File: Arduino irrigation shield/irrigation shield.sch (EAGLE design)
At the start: 3 parts, among them IC1 74LS595N, U1 ARDUINOR3-DIMENSION

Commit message: work in progress
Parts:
- added DZ1: LB10, led:LB10
- added R1: 4.7k, resistor:R-US_0207/7
- added S1: Next Zone, switch-omron:10-XX
- added SJ1, SJ2, SJ3, SJ4, SJ5, SJ6, SJ7: (no value), jumper:SJ
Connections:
- new net N$1: IC1A.SCK, U1.D6
- new net N$2: IC1A.RCK, U1.D5
- new net N$3: IC1A.SER, U1.D4
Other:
- moved on the sheet: IC1
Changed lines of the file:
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@@
 <part name="IC1" library="74xx-us" deviceset="74*595" device="N" technology="LS"/>
 <part name="T1" library="transistor" deviceset="*-NPN-" device="TO92"/>
+<part name="R1" library="resistor" deviceset="R-US_" device="0207/7" value="4.7k"/>
+<part name="DZ1" library="led" deviceset="LB10" device=""/>
+<part name="SJ1" library="jumper" deviceset="SJ" device=""/>
+<part name="SJ2" library="jumper" deviceset="SJ" device=""/>
+<part name="SJ3" library="jumper" deviceset="SJ" device=""/>
+<part name="SJ4" library="jumper" deviceset="SJ" device=""/>
+<part name="SJ5" library="jumper" deviceset="SJ" device=""/>
+<part name="SJ6" library="jumper" deviceset="SJ" device=""/>
+<part name="SJ7" library="jumper" deviceset="SJ" device=""/>
+<part name="S1" library="switch-omron" deviceset="10-XX" device="" value="Next Zone"/>
 </parts>
 <sheets>
@@
 <instances>
 <instance part="U1" gate="G$1" x="10.16" y="58.42"/>
-<instance part="IC1" gate="A" x="86.36" y="66.04"/>
+<instance part="IC1" gate="A" x="20.32" y="116.84" rot="R90"/>
 <instance part="T1" gate="G$1" x="71.12" y="30.48"/>
+<instance part="R1" gate="G$1" x="58.42" y="30.48"/>
+<instance part="DZ1" gate="-1" x="48.26" y="91.44"/>
+<instance part="DZ1" gate="-2" x="63.5" y="91.44"/>
+<instance part="DZ1" gate="-3" x="78.74" y="91.44"/>
+<instance part="DZ1" gate="-4" x="93.98" y="91.44"/>
+<instance part="DZ1" gate="-5" x="109.22" y="91.44"/>
+<instance part="DZ1" gate="-6" x="48.26" y="73.66"/>
+<instance part="DZ1" gate="-7" x="63.5" y="73.66"/>
+<instance part="DZ1" gate="-8" x="78.74" y="73.66"/>
+<instance part="DZ1" gate="-9" x="93.98" y="73.66"/>
+<instance part="DZ1" gate="-10" x="109.22" y="73.66"/>
+<instance part="SJ1" gate="1" x="48.26" y="63.5"/>
+<instance part="SJ2" gate="1" x="60.96" y="63.5"/>
+<instance part="SJ3" gate="1" x="73.66" y="63.5"/>
+<instance part="SJ4" gate="1" x="86.36" y="63.5"/>
+<instance part="SJ5" gate="1" x="99.06" y="63.5"/>
+<instance part="SJ6" gate="1" x="111.76" y="63.5"/>
+<instance part="SJ7" gate="1" x="124.46" y="63.5"/>
+<instance part="S1" gate="1" x="-35.56" y="109.22"/>
 </instances>
 <busses>
 </busses>
 <nets>
+<net name="N$1" class="0">
+<segment>
+<pinref part="U1" gate="G$1" pin="D6"/>
+<pinref part="IC1" gate="A" pin="SCK"/>
+<wire x1="15.24" y1="88.9" x2="15.24" y2="106.68" width="0.1524" layer="91"/>
+</segment>
+</net>
+<net name="N$2" class="0">
+<segment>
+<pinref part="U1" gate="G$1" pin="D5"/>
+<wire x1="17.78" y1="88.9" x2="17.78" y2="99.06" width="0.1524" layer="91"/>
+<wire x1="17.78" y1="99.06" x2="22.86" y2="99.06" width="0.1524" layer="91"/>
+<pinref part="IC1" gate="A" pin="RCK"/>
+<wire x1="22.86" y1="99.06" x2="22.86" y2="106.68" width="0.1524" layer="91"/>
+</segment>
+</net>
+<net name="N$3" class="0">
+<segment>
+<pinref part="U1" gate="G$1" pin="D4"/>
+<wire x1="20.32" y1="88.9" x2="20.32" y2="96.52" width="0.1524" layer="91"/>
+<wire x1="20.32" y1="96.52" x2="10.16" y2="96.52" width="0.1524" layer="91"/>
+<pinref part="IC1" gate="A" pin="SER"/>
+<wire x1="10.16" y1="96.52" x2="10.16" y2="106.68" width="0.1524" layer="91"/>
+</segment>
+</net>
 </nets>
 </sheet>

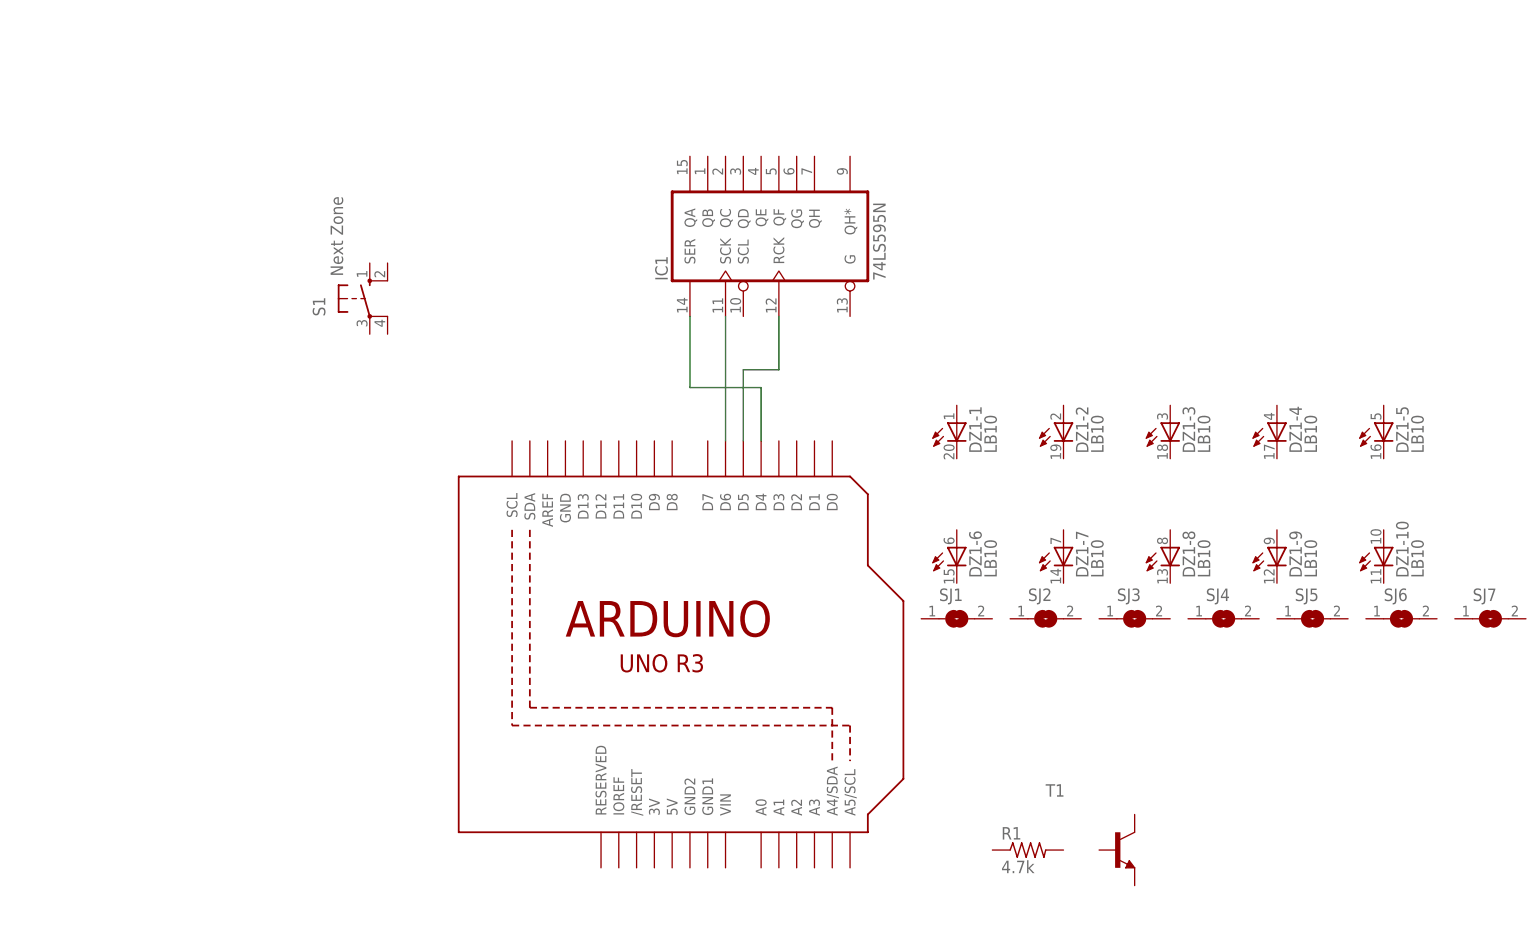
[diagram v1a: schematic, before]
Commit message: wired up shift reg and button
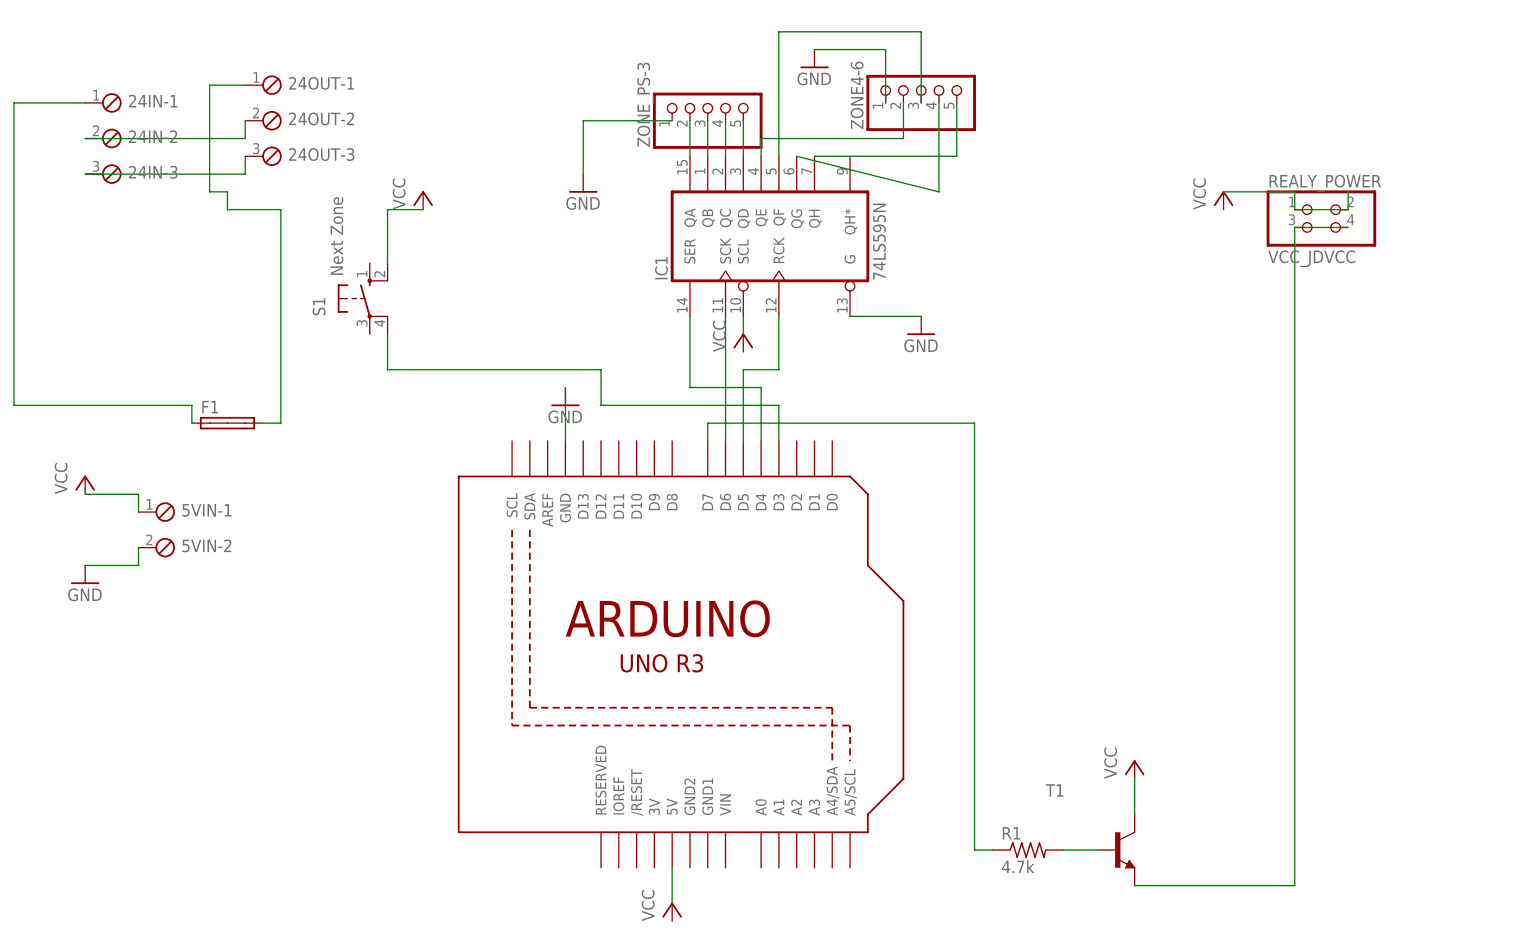
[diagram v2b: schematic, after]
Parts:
- removed DZ1: LB10, led:LB10
- removed SJ1, SJ2, SJ3, SJ4, SJ5, SJ6, SJ7: (no value), jumper:SJ
- added 24IN, 24OUT: (no value), con-phoenix-254:MPT3
- added 5VIN: (no value), con-phoenix-254:MPT2
- added F1: (no value), fuse:SH32
- added REALY_POWER: VCC_JDVCC, pinhead:PINHD-2X2
- added ZONE4-6, ZONE_PS-3: (no value), pinhead:PINHD-1X5
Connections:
- new net GND: 5VIN-2.1, IC1A.G, U1.GND, ZONE4-6.1, ZONE_PS-3.1
- new net N$10: U1.5V
- new net N$11: 24IN-1.1, F1.1A
- new net N$12: REALY_POWER.3, REALY_POWER.4, T1.E
- new net N$13: IC1A.QE, ZONE4-6.2
- new net N$14: IC1A.QF, ZONE4-6.3
- new net N$15: IC1A.QG, ZONE4-6.4
- new net N$16: IC1A.QH, ZONE4-6.5
- new net N$17: REALY_POWER.1, REALY_POWER.2
- new net N$18: 24OUT-1.1, F1.2A
- new net N$19: 24IN-2.1, 24OUT-2.1
- new net N$20: 24IN-3.1, 24OUT-3.1
- new net N$21: IC1A.SCL
- new net N$22: S1.P1, U1.D3
- new net N$4: R1.2, T1.B
- new net N$5: R1.1, U1.D7
- new net N$6: IC1A.QA, ZONE_PS-3.2
- new net N$7: IC1A.QB, ZONE_PS-3.3
- new net N$8: IC1A.QC, ZONE_PS-3.4
- new net N$9: IC1A.QD, ZONE_PS-3.5
- new net VCC: 5VIN-1.1, S1.S1, T1.C

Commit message: RTC and ESP8266 header added
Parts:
- added JP1: ESP8266, adafruit:PINHD-2X4
- added JP2: LevShiftHI, adafruit:PINHD-1X6
- added JP3: LevShoftLO, adafruit:PINHD-1X6
- added RTC: RTC, pinhead:PINHD-1X6/90
- 24IN: value (none) -> 24V_PSU
- 24OUT: value (none) -> Solenoid
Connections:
- new net N$23: RTC.3, U1.SCL
- new net N$24: JP2.6, U1.D0
- net GND: now also RTC.6
- net N$10: now also JP2.5, U1.D1; no longer U1.5V
- net N$21: now also RTC.4, U1.SDA; no longer IC1A.SCL
- net VCC: now also IC1A.SCL, RTC.5, U1.5V
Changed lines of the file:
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@@
 <part name="P+2" library="supply1" deviceset="VCC" device=""/>
 <part name="P+3" library="supply1" deviceset="VCC" device=""/>
-<part name="24IN" library="con-phoenix-254" deviceset="MPT3" device=""/>
-<part name="24OUT" library="con-phoenix-254" deviceset="MPT3" device=""/>
+<part name="24IN" library="con-phoenix-254" deviceset="MPT3" device="" value="24V_PSU"/>
+<part name="24OUT" library="con-phoenix-254" deviceset="MPT3" device="" value="Solenoid"/>
 <part name="GND3" library="supply1" deviceset="GND" device=""/>
 <part name="P+4" library="supply1" deviceset="VCC" device=""/>
@@
 <part name="P+6" library="supply1" deviceset="VCC" device=""/>
 <part name="GND5" library="supply1" deviceset="GND" device=""/>
+<part name="RTC" library="pinhead" deviceset="PINHD-1X6" device="/90" value="RTC"/>
+<part name="JP1" library="adafruit" deviceset="PINHD-2X4" device="" value="ESP8266"/>
+<part name="JP2" library="adafruit" deviceset="PINHD-1X6" device="" value="LevShiftHI"/>
+<part name="JP3" library="adafruit" deviceset="PINHD-1X6" device="" value="LevShoftLO"/>
 </parts>
 <sheets>
@@
 <instance part="P+6" gate="VCC" x="-76.2" y="83.82"/>
 <instance part="GND5" gate="1" x="-76.2" y="68.58"/>
+<instance part="RTC" gate="A" x="-43.18" y="55.88"/>
+<instance part="JP1" gate="A" x="86.36" y="96.52"/>
+<instance part="JP2" gate="A" x="60.96" y="96.52"/>
+<instance part="JP3" gate="A" x="71.12" y="96.52"/>
 </instances>
 <busses>
@@
 <wire x1="-76.2" y1="71.12" x2="-68.58" y2="71.12" width="0.1524" layer="91"/>
 <wire x1="-68.58" y1="71.12" x2="-68.58" y2="73.66" width="0.1524" layer="91"/>
-</segment>
-</net>
-<net name="N$10" class="0">
-<segment>
-<pinref part="U1" gate="G$1" pin="5V"/>
-<wire x1="7.62" y1="22.86" x2="7.62" y2="27.94" width="0.1524" layer="91"/>
+<pinref part="RTC" gate="A" pin="6"/>
+<wire x1="-45.72" y1="50.8" x2="-68.58" y2="50.8" width="0.1524" layer="91"/>
+<wire x1="-68.58" y1="50.8" x2="-68.58" y2="71.12" width="0.1524" layer="91"/>
 </segment>
 </net>
@@
 <wire x1="-76.2" y1="81.28" x2="-68.58" y2="81.28" width="0.1524" layer="91"/>
 <wire x1="-68.58" y1="81.28" x2="-68.58" y2="78.74" width="0.1524" layer="91"/>
+<pinref part="RTC" gate="A" pin="5"/>
+<wire x1="-45.72" y1="53.34" x2="-86.36" y2="53.34" width="0.1524" layer="91"/>
+<wire x1="-86.36" y1="53.34" x2="-86.36" y2="78.74" width="0.1524" layer="91"/>
+<wire x1="-86.36" y1="78.74" x2="-68.58" y2="78.74" width="0.1524" layer="91"/>
+</segment>
+<segment>
+<pinref part="U1" gate="G$1" pin="5V"/>
+<wire x1="7.62" y1="22.86" x2="7.62" y2="27.94" width="0.1524" layer="91"/>
+</segment>
+<segment>
+<pinref part="IC1" gate="A" pin="SCL"/>
+<wire x1="17.78" y1="106.68" x2="17.78" y2="104.14" width="0.1524" layer="91"/>
 </segment>
 </net>
@@
 <net name="N$16" class="0">
 <segment>
+<pinref part="ZONE4-6" gate="A" pin="5"/>
 <pinref part="IC1" gate="A" pin="QH"/>
-<wire x1="27.94" y1="129.54" x2="48.26" y2="129.54" width="0.1524" layer="91"/>
-<pinref part="ZONE4-6" gate="A" pin="5"/>
-<wire x1="48.26" y1="129.54" x2="48.26" y2="137.16" width="0.1524" layer="91"/>
+<wire x1="27.94" y1="129.54" x2="27.94" y2="149.86" width="0.1524" layer="91"/>
+<wire x1="27.94" y1="149.86" x2="48.26" y2="149.86" width="0.1524" layer="91"/>
+<wire x1="48.26" y1="149.86" x2="48.26" y2="137.16" width="0.1524" layer="91"/>
 </segment>
 </net>
@@
 </segment>
 </net>
-<net name="N$21" class="0">
-<segment>
-<pinref part="IC1" gate="A" pin="SCL"/>
-<wire x1="17.78" y1="106.68" x2="17.78" y2="104.14" width="0.1524" layer="91"/>
-</segment>
-</net>
 <net name="N$22" class="0">
 <segment>
@@
 </segment>
 </net>
+<net name="N$21" class="0">
+<segment>
+<pinref part="RTC" gate="A" pin="4"/>
+<wire x1="-45.72" y1="55.88" x2="-35.56" y2="55.88" width="0.1524" layer="91"/>
+<wire x1="-35.56" y1="55.88" x2="-35.56" y2="93.98" width="0.1524" layer="91"/>
+<pinref part="U1" gate="G$1" pin="SDA"/>
+<wire x1="-35.56" y1="93.98" x2="-12.7" y2="93.98" width="0.1524" layer="91"/>
+<wire x1="-12.7" y1="93.98" x2="-12.7" y2="88.9" width="0.1524" layer="91"/>
+</segment>
+</net>
+<net name="N$23" class="0">
+<segment>
+<pinref part="RTC" gate="A" pin="3"/>
+<wire x1="-45.72" y1="58.42" x2="-30.48" y2="58.42" width="0.1524" layer="91"/>
+<wire x1="-30.48" y1="58.42" x2="-30.48" y2="91.44" width="0.1524" layer="91"/>
+<wire x1="-30.48" y1="91.44" x2="-15.24" y2="91.44" width="0.1524" layer="91"/>
+<pinref part="U1" gate="G$1" pin="SCL"/>
+<wire x1="-15.24" y1="91.44" x2="-15.24" y2="88.9" width="0.1524" layer="91"/>
+</segment>
+</net>
+<net name="N$10" class="0">
+<segment>
+<pinref part="JP2" gate="A" pin="5"/>
+<pinref part="U1" gate="G$1" pin="D1"/>
+<wire x1="58.42" y1="93.98" x2="27.94" y2="93.98" width="0.1524" layer="91"/>
+<wire x1="27.94" y1="93.98" x2="27.94" y2="88.9" width="0.1524" layer="91"/>
+</segment>
+</net>
+<net name="N$24" class="0">
+<segment>
+<pinref part="U1" gate="G$1" pin="D0"/>
+<pinref part="JP2" gate="A" pin="6"/>
+<wire x1="30.48" y1="88.9" x2="58.42" y2="88.9" width="0.1524" layer="91"/>
+<wire x1="58.42" y1="88.9" x2="58.42" y2="91.44" width="0.1524" layer="91"/>
+</segment>
+</net>
 </nets>
 </sheet>
 </sheets>
+<errors>
+</errors>
 </schematic>
 </drawing>
